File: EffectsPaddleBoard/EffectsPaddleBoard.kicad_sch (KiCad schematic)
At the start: 47 parts, among them J3 Barrel_Jack, U2 TPS54233, U4 TPS54233

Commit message: Corrections, see comments
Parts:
- C25, C26, C28, C29: Distributer Link (none) -> https://www.mouser.ch/ProductDetail/Murata-Electronics/GRM0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; Manufacturer (none) -> Murata Electronics; Manufacturer Part Number (none) -> GRM0225C1C221JA02L
- C31, C32, C42, C43: Distributer Link (none) -> https://www.mouser.ch/ProductDetail/Murata-Electronics/GRM3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; Manufacturer (none) -> Murata Electronics; Manufacturer Part Number (none) -> GRM319R71C105KAA3J
- D2, D3: Distributer Link (none) -> https://www.mouser.ch/ProductDetail/Diodes-Incorporated/B23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; Manufacturer (none) -> Diodes Incorporated; Manufacturer Part Number (none) -> B230-13-F
- D4: Distributer Link (none) -> https://www.mouser.ch/ProductDetail/Wurth-Elektronik/150040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; Manufacturer (none) -> Wurth Elektronik; Manufacturer Part Number (none) -> 150040RS73240
- FB1, FB2: value 600 -> 100; Distributer Link (none) -> https://www.mouser.ch/ProductDetail/Murata-Electronics/BLM1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; Manufacturer (none) -> Murata Electronics; Manufacturer Part Number (none) -> BLM18KG121TN1D
- L1, L2: footprint Inductor_SMD:L_0603_1608Metric -> Inductor_SMD:L_0805_2012Metric; Distributer Link (none) -> https://www.mouser.ch/ProductDetail/Murata-Electronics/LQM2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; Manufacturer (none) -> Murata Electronics; Manufacturer Part Number (none) -> LQM21DN150M70L
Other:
- note added: "Get down with LDOs"

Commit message: Corrected the board, now all parts should be right
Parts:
- removed C21: 10u, Capacitor_SMD:C_1206_3216Metric, symbol Device:C_Small
- removed C22: 15n, Capacitor_SMD:C_0402_1005Metric, symbol Device:C_Small
- removed C23: 100n, Capacitor_SMD:C_0402_1005Metric, symbol Device:C_Small
- removed C24, C40: 470u, Capacitor_SMD:CP_Elec_8x10.5, symbol Device:C_Polarized
- removed C25, C26: 220p, Capacitor_SMD:C_0402_1005Metric, symbol Device:C_Small
- removed C30: 10u, Capacitor_SMD:C_1206_3216Metric, symbol Device:C
- removed C31, C32: 1u, Capacitor_SMD:C_1206_3216Metric, symbol Device:C
- removed D2: B230, Diode_SMD:D_SMB, symbol Diode:B230
- removed FB1: 100, Inductor_SMD:L_0603_1608Metric, symbol Device:FerriteBead
- removed L1: 15u, Inductor_SMD:L_0805_2012Metric, symbol Device:L_Small
- removed R21: 4k7, Resistor_SMD:R_1206_3216Metric, symbol Device:R_Small
- removed R22: 3k9, Resistor_SMD:R_1206_3216Metric, symbol Device:R_Small
- removed R5: 332k, Resistor_SMD:R_1206_3216Metric, symbol Device:R_Small
- removed R6: 68.1k, Resistor_SMD:R_1206_3216Metric, symbol Device:R_Small
- removed R7: 10.2k, Resistor_SMD:R_1206_3216Metric, symbol Device:R_Small
- removed R8: 3.24k, Resistor_SMD:R_1206_3216Metric, symbol Device:R_Small
- removed R9: 30.9k, Resistor_SMD:R_1206_3216Metric, symbol Device:R_Small
- removed TP1: TestPoint, Connector_Pin:Pin_D1.3mm_L11.0mm, symbol Connector:TestPoint
- removed U2: TPS54233, Package_SO:SOIC-8_3.9x4.9mm_P1.27mm, symbol Regulator_Switching:TPS54233
- added C19 (x6): 1u, Capacitor_SMD:C_0805_2012Metric, symbol Device:C
- added U2, U5: TPS7A0533PDBZ, Package_TO_SOT_SMD:SOT-23, symbol Regulator_Linear:TPS7A0533PDBZ
- added U8: TPS7A0518PDBZ, Package_TO_SOT_SMD:SOT-23, symbol Regulator_Linear:TPS7A0518PDBZ
- C27, C41, C42, C43: footprint Capacitor_SMD:C_1206_3216Metric -> Capacitor_SMD:C_0805_2012Metric
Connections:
- net +1V8: now also C19.2, U8.2 (VO)
- net +3.3V: now also C19.2, U2.2 (VO)
- net +3.3VA: now also C19.2, U5.2 (VO)
- net +5V: now also C19.2, C19.2, C19.2, U2.3 (VI), U5.3 (VI), U8.3 (VI)
- net GND: now also C19.1, C19.1, C19.1, C19.1, C19.1, C19.1, U2.1 (GND), U5.1 (GND), U8.1 (GND)
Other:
- note removed: "Get down with LDOs"
- moved on the sheet: C41, C42, C43, FB2

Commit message: Layout completed
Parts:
- added D2: LED, LED_SMD:LED_0402_1005Metric, symbol Device:LED
- added R7: 220, Resistor_SMD:R_0402_1005Metric, symbol Device:R
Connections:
- net +5V: now also R7.2
- net GND: now also D2.1 (K)
- new net: D2.2 (A), R7.1
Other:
- note removed: "May want to add a LED indicator for 5V"
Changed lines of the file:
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@@
   (junction (at 177.8 60.325) (diameter 0) (color 0 0 0 0)
   )
-  (junction (at 52.07 109.855) (diameter 0) (color 0 0 0 0)
-  )
   (junction (at 85.09 45.72) (diameter 0) (color 0 0 0 0)
   )
@@
     (stroke (width 0) (type default))
   )
+  (wire (pts (xy 99.06 142.24) (xy 99.06 147.32))
+    (stroke (width 0) (type default))
+  )
   (wire (pts (xy 142.24 44.45) (xy 142.24 60.325))
     (stroke (width 0) (type default))
@@
     (stroke (width 0) (type default))
   )
-  (wire (pts (xy 52.07 109.855) (xy 71.12 109.855))
-    (stroke (width 0) (type default))
-  )
   (wire (pts (xy 32.385 174.625) (xy 32.385 170.815))
     (stroke (width 0) (type default))
@@
     (stroke (width 0) (type default))
   )
+  (wire (pts (xy 99.06 128.27) (xy 99.06 134.62))
+    (stroke (width 0) (type default))
+  )
   (wire (pts (xy 106.68 78.105) (xy 106.68 75.565))
     (stroke (width 0) (type default))
   )
+  (wire (pts (xy 90.805 128.27) (xy 99.06 128.27))
+    (stroke (width 0) (type default))
+  )
   (wire (pts (xy 63.5 34.29) (xy 85.09 34.29))
     (stroke (width 0) (type default))
@@
     (stroke (width 0) (type default))
   )
+  (wire (pts (xy 79.375 128.27) (xy 83.185 128.27))
+    (stroke (width 0) (type default))
+  )
   (wire (pts (xy 159.385 165.1) (xy 174.625 165.1))
     (stroke (width 0) (type default))
@@
     (stroke (width 0) (type default))
   )
+  (wire (pts (xy 79.375 122.555) (xy 79.375 128.27))
+    (stroke (width 0) (type default))
+  )
   (wire (pts (xy 62.865 170.815) (xy 62.865 174.625))
     (stroke (width 0) (type default))
@@
   (wire (pts (xy 186.055 121.285) (xy 173.99 121.285))
     (stroke (width 0) (type default))
-  )
-  (text "May want to add a LED indicator for 5V" (at 17.78 92.71 0)
-    (effects (font (size 1.27 1.27)) (justify left bottom))
   )
   (label "fb5v" (at 155.575 60.325 0) (fields_autoplaced)
@@
     )
   )
+  (symbol (lib_id "Device:LED") (at 99.06 138.43 90) (unit 1)
+    (in_bom yes) (on_board yes) (dnp no) (fields_autoplaced)
+    (property "Reference" "D2" (at 102.87 139.3825 90)
+      (effects (font (size 1.27 1.27)) (justify right))
+    )
+    (property "Value" "LED" (at 102.87 141.9225 90)
+      (effects (font (size 1.27 1.27)) (justify right))
+    )
+    (property "Footprint" "LED_SMD:LED_0402_1005Metric" (at 99.06 138.43 0)
+      (effects (font (size 1.27 1.27)) hide)
+    )
+    (property "Datasheet" "~" (at 99.06 138.43 0)
+      (effects (font (size 1.27 1.27)) hide)
+    )
+    (property "Sim.Enable" "0" (at 99.06 138.43 0)
+      (effects (font (size 1.27 1.27)) hide)
+    )
+    (property "Distributer Link" "https://www.mouser.ch/ProductDetail/Wurth-Elektronik/150040RS73240?qs=8Aam6%252B7C6HGMiInmnlrBiw%3D%3D" (at 99.06 138.43 0)
+      (effects (font (size 1.27 1.27)) hide)
+    )
+    (property "Manufacturer" "Wurth Elektronik" (at 99.06 138.43 0)
+      (effects (font (size 1.27 1.27)) hide)
+    )
+    (property "Manufacturer Part Number" "150040RS73240" (at 99.06 138.43 0)
+      (effects (font (size 1.27 1.27)) hide)
+    )
+    (pin "1")
+    (pin "2")
+    (instances
+      (project "EffectsPaddleBoard"
+        (path "/40bb1606-5207-4492-95b9-876879aab2b4"
+          (reference "D2") (unit 1)
+        )
+      )
+    )
+  )
   (symbol (lib_id "Device:C") (at 32.385 178.435 0) (unit 1)
     (in_bom yes) (on_board yes) (dnp no) (fields_autoplaced)
@@
         (path "/40bb1606-5207-4492-95b9-876879aab2b4"
           (reference "C27") (unit 1)
+        )
+      )
+    )
+  )
+  (symbol (lib_id "Device:R") (at 86.995 128.27 270) (unit 1)
+    (in_bom yes) (on_board yes) (dnp no) (fields_autoplaced)
+    (property "Reference" "R7" (at 86.995 123.19 90)
+      (effects (font (size 1.27 1.27)))
+    )
+    (property "Value" "220" (at 86.995 125.73 90)
+      (effects (font (size 1.27 1.27)))
+    )
+    (property "Footprint" "Resistor_SMD:R_0402_1005Metric" (at 86.995 126.492 90)
+      (effects (font (size 1.27 1.27)) hide)
+    )
+    (property "Datasheet" "~" (at 86.995 128.27 0)
+      (effects (font (size 1.27 1.27)) hide)
+    )
+    (property "Sim.Enable" "0" (at 86.995 128.27 0)
+      (effects (font (size 1.27 1.27)) hide)
+    )
+    (property "Distributer Link" "" (at 86.995 128.27 0)
+      (effects (font (size 1.27 1.27)) hide)
+    )
+    (property "Manufacturer" "" (at 86.995 128.27 0)
+      (effects (font (size 1.27 1.27)) hide)
+    )
+    (property "Manufacturer Part Number" "" (at 86.995 128.27 0)
+      (effects (font (size 1.27 1.27)) hide)
+    )
+    (pin "1")
+    (pin "2")
+    (instances
+      (project "EffectsPaddleBoard"
+        (path "/40bb1606-5207-4492-95b9-876879aab2b4"
+          (reference "R7") (unit 1)
         )
       )
@@
     )
   )
+  (symbol (lib_id "power:+5V") (at 79.375 122.555 0) (unit 1)
+    (in_bom yes) (on_board yes) (dnp no) (fields_autoplaced)
+    (property "Reference" "#PWR034" (at 79.375 126.365 0)
+      (effects (font (size 1.27 1.27)) hide)
+    )
+    (property "Value" "+5V" (at 79.375 118.745 0)
+      (effects (font (size 1.27 1.27)))
+    )
+    (property "Footprint" "" (at 79.375 122.555 0)
+      (effects (font (size 1.27 1.27)) hide)
+    )
+    (property "Datasheet" "" (at 79.375 122.555 0)
+      (effects (font (size 1.27 1.27)) hide)
+    )
+    (property "Sim.Enable" "0" (at 79.375 122.555 0)
+      (effects (font (size 1.27 1.27)) hide)
+    )
+    (pin "1")
+    (instances
+      (project "EffectsPaddleBoard"
+        (path "/40bb1606-5207-4492-95b9-876879aab2b4"
+          (reference "#PWR034") (unit 1)
+        )
+      )
+    )
+  )
   (symbol (lib_id "power:GND") (at 121.285 55.245 0) (unit 1)
     (in_bom yes) (on_board yes) (dnp no) (fields_autoplaced)
@@
         )
       )
+    )
+  )
+  (symbol (lib_id "power:GND") (at 99.06 147.32 0) (unit 1)
+    (in_bom yes) (on_board yes) (dnp no) (fields_autoplaced)
+    (property "Reference" "#PWR035" (at 99.06 153.67 0)
+      (effects (font (size 1.27 1.27)) hide)
+    )
+    (property "Value" "GND" (at 99.06 152.4 0)
+      (effects (font (size 1.27 1.27)))
+    )
+    (property "Footprint" "" (at 99.06 147.32 0)
+      (effects (font (size 1.27 1.27)) hide)
+    )
+    (property "Datasheet" "" (at 99.06 147.32 0)
+      (effects (font (size 1.27 1.27)) hide)
+    )
+    (property "Sim.Enable" "0" (at 99.06 147.32 0)
+      (effects (font (size 1.27 1.27)) hide)
+    )
+    (pin "1")
+    (instances
+      (project "EffectsPaddleBoard"
+        (path "/40bb1606-5207-4492-95b9-876879aab2b4"
+          (reference "#PWR035") (unit 1)
+        )
+      )

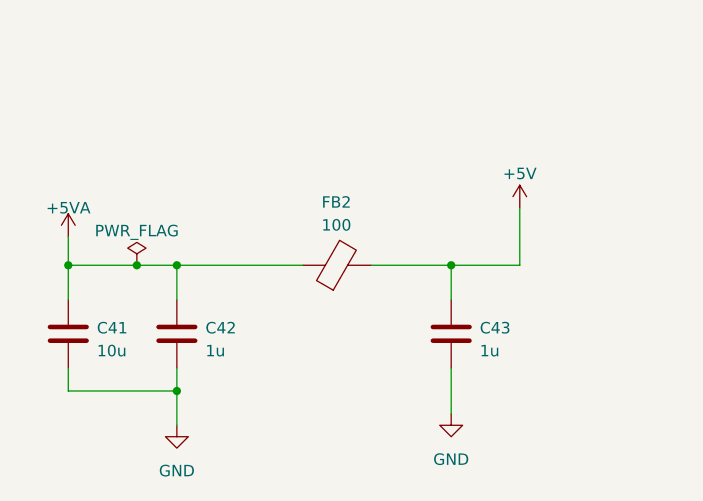
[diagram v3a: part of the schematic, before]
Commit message: Added filter simulation and last copperfills on front copper (ugly)
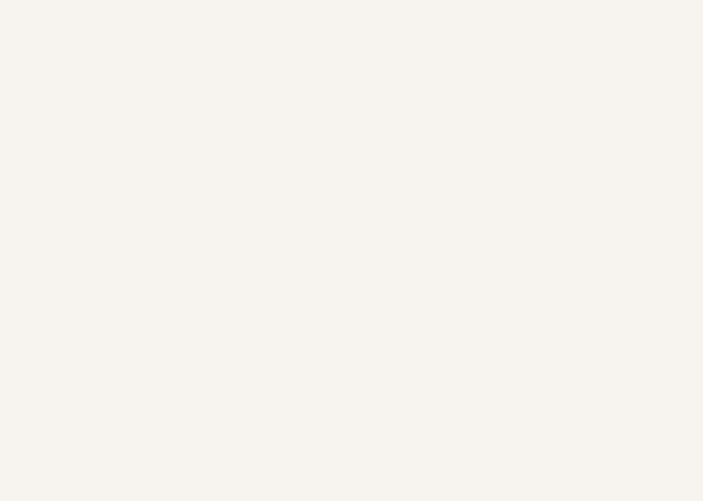
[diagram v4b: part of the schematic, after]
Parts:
- removed C41: 10u, Capacitor_SMD:C_0805_2012Metric, symbol Device:C
- removed C42, C43: 1u, Capacitor_SMD:C_0805_2012Metric, symbol Device:C
- removed FB2: 100, Inductor_SMD:L_0603_1608Metric, symbol Device:FerriteBead

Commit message: Added all parts
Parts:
- C19: Distributer Link (none) -> https://www.mouser.ch/ProductDetail/Murata-Electronics/GRM2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; Manufacturer (none) -> Murata Electronics; Manufacturer Part Number (none) -> GRM21BR71C105KA01K
- C27: Distributer Link https://www.mouser.ch/ProductDetail/Murata-Electronics/GRM3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 -> https://www.mouser.ch/ProductDetail/Murata-Electronics/GCM2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; Manufacturer Part Number GRM31CR71C106KAC7L -> GCM21BC71E106KE36K
- C38: Distributer Link https://www.mouser.ch/ProductDetail/Murata-Electronics/GRM152R61A104KE19D?qs=IPQhFcwEUOjgOs7G%2Fz457g%3D%3D -> https://www.mouser.ch/ProductDetail/Murata-Electronics/GRM155R61C104KA88J?qs=sGAEpiMZZMsh%252B1woXyUXj8YF%2FGivH5Kx4uStnYyl8jU%3D; Manufacturer Part Number GRM152R61A104KE19D -> GRM155R61C104KA88J
- R10: Distributer Link (none) -> https://www.mouser.ch/ProductDetail/Vishay-Dale/TNPW1206332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; Manufacturer (none) -> Vishay / Dale; Manufacturer Part Number (none) -> TNPW1206332KBEEA
- R11: Distributer Link (none) -> https://www.mouser.ch/ProductDetail/Vishay-Dale/TNPW120668K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; Manufacturer (none) -> Vishay / Dale; Manufacturer Part Number (none) -> TNPW120668K1BEEN
- R12: Distributer Link (none) -> https://www.mouser.ch/ProductDetail/Vishay-Dale/TNPW120630K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; Manufacturer (none) -> Vishay / Dale; Manufacturer Part Number (none) -> TNPW120630K9BEEN
- R13: Distributer Link (none) -> https://www.mouser.ch/ProductDetail/Vishay-Dale/TNPW120610K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; Manufacturer (none) -> Vishay / Dale; Manufacturer Part Number (none) -> TNPW120610K0BETY
- R14, R15: Distributer Link (none) -> https://www.mouser.ch/ProductDetail/Vishay-Dale/TNPW12063K9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; Manufacturer (none) -> Vishay / Dale; Manufacturer Part Number (none) -> TNPW12063K90BEEA
- R32, R7: Distributer Link (none) -> https://www.mouser.ch/ProductDetail/Vishay-Beyschlag/MCS040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; Manufacturer (none) -> Vishay / Beyschlag; Manufacturer Part Number (none) -> MCS04020C2200FE000
- U4: Distributer Link (none) -> https://www.mouser.ch/ProductDetail/Texas-Instruments/TPS54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; Manufacturer (none) -> Texas Instruments; Manufacturer Part Number (none) -> TPS54233DRG4
